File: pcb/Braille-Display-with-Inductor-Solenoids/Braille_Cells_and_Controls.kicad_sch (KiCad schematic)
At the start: 6 parts, among them U26 74HC595, U27 74HC595, U28 74HC595, U29 74HC595, U30 74HC595, U31 74HC595

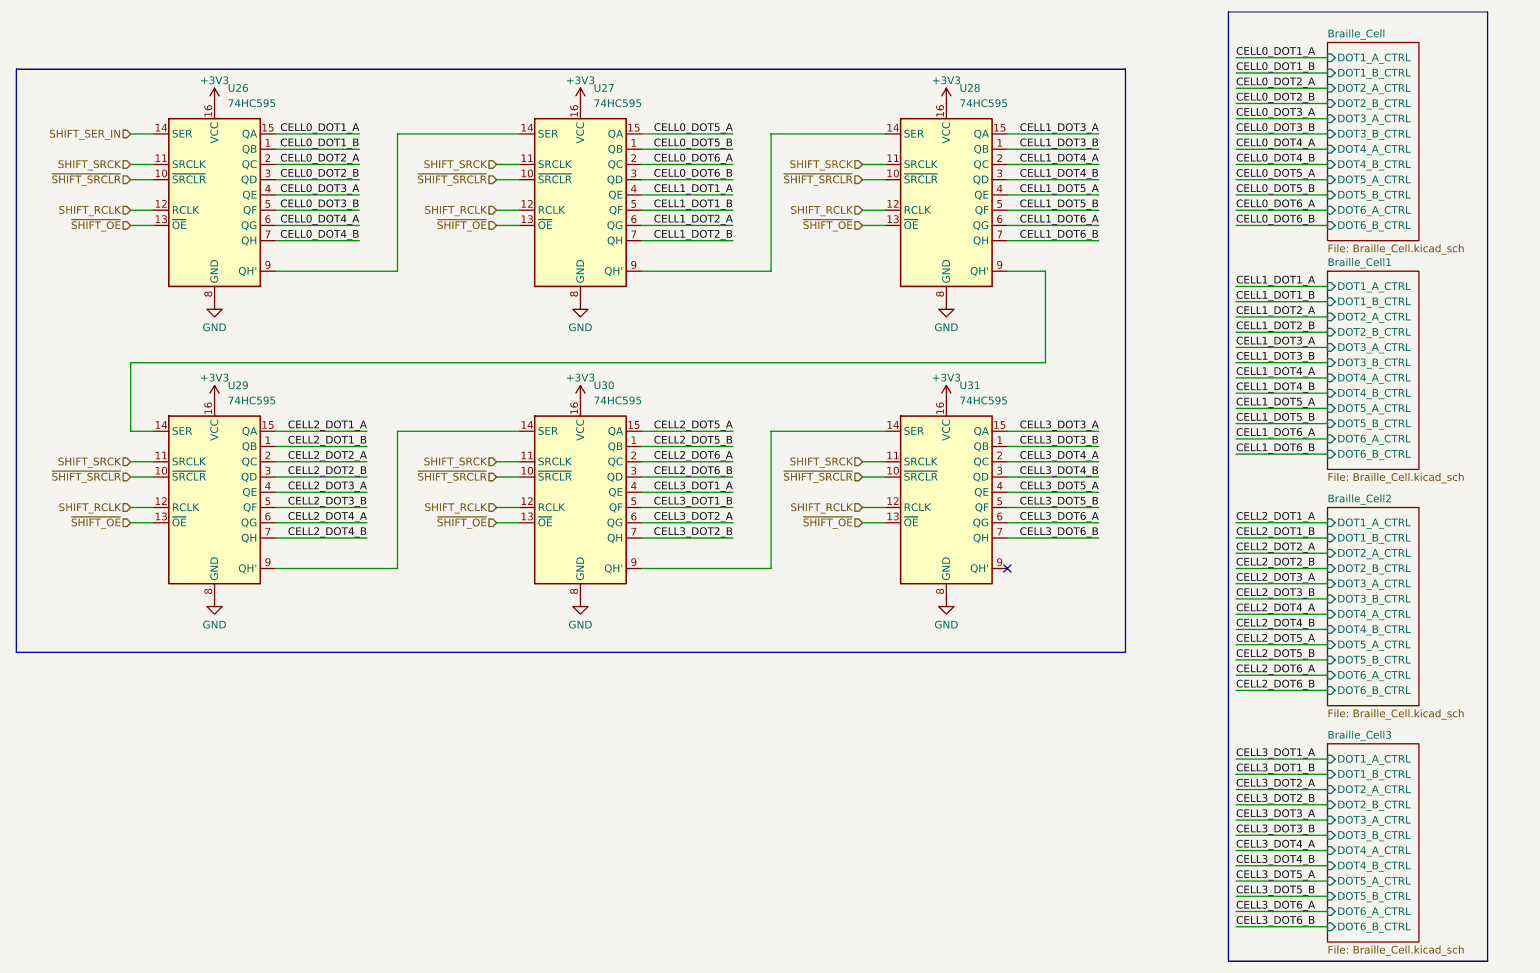
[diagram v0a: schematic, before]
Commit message: WIP (Rev3): Switch to 2 inductors per cell
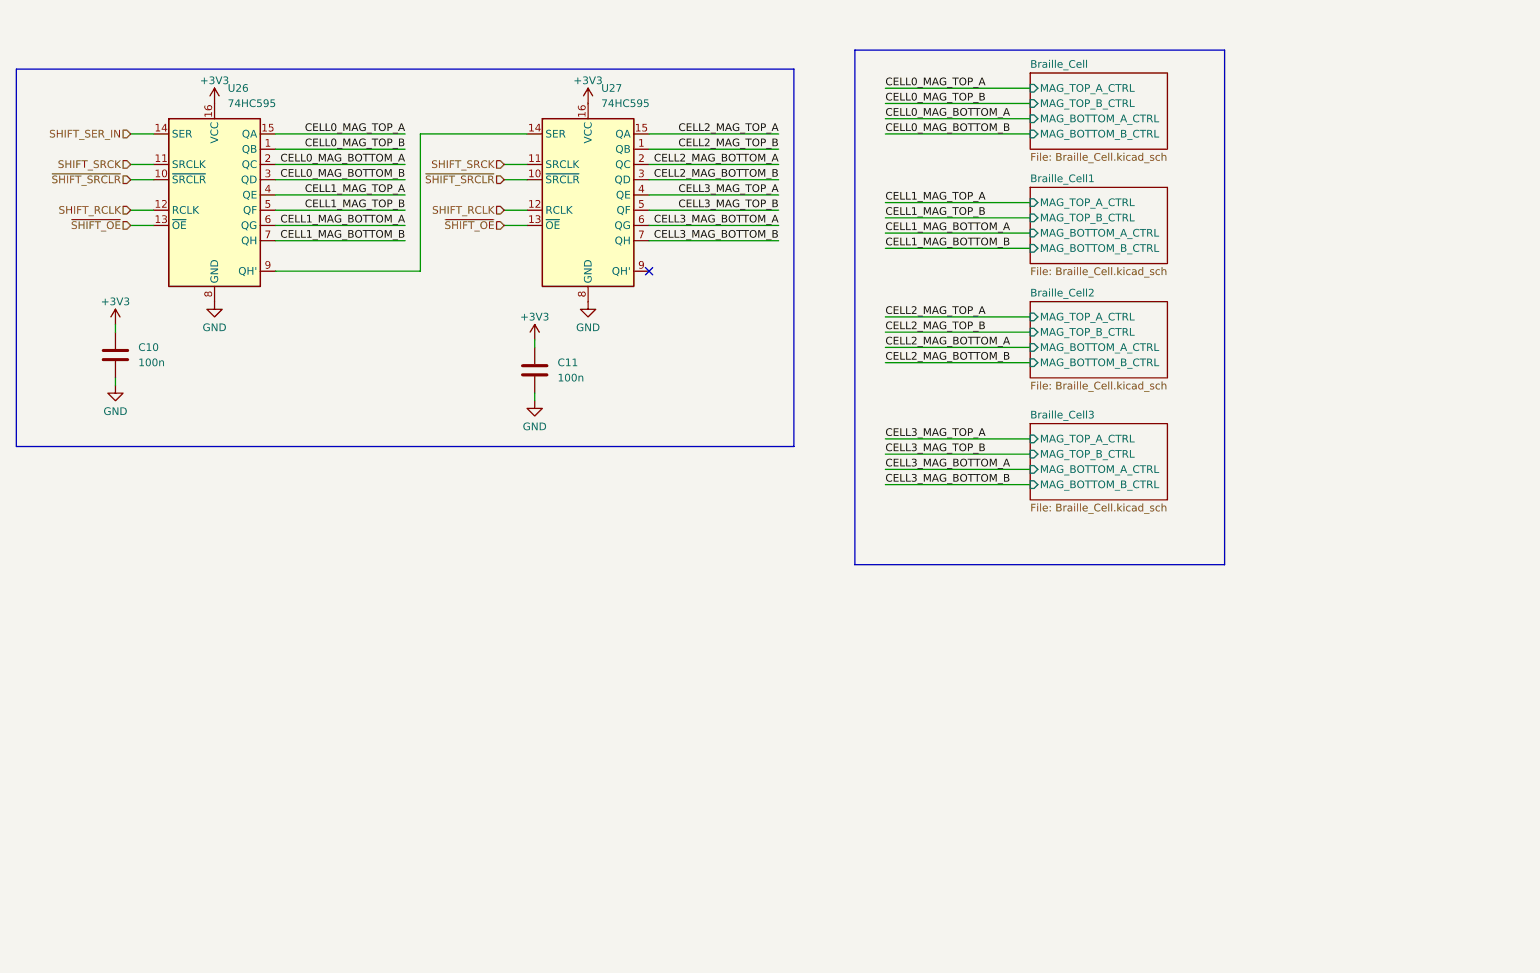
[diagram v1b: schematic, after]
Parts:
- removed U28, U29, U30, U31: 74HC595, Package_SO:SOP-16_3.9x9.9mm_P1.27mm, symbol 74xx:74HC595
- added C10, C11: 100n, Capacitor_SMD:C_1206_3216Metric_Pad1.33x1.80mm_HandSolder, symbol Device:C
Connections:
- net +3V3: now also C10.1, C11.1
- net GND: now also C10.2, C11.2
- net CELL0_DOT1_A renamed CELL0_MAG_TOP_A
- net CELL0_DOT1_B renamed CELL0_MAG_TOP_B
- net CELL0_DOT2_A renamed CELL0_MAG_BOTTOM_A
- net CELL0_DOT2_B renamed CELL0_MAG_BOTTOM_B
- net CELL0_DOT3_A renamed CELL1_MAG_TOP_A
- net CELL0_DOT3_B renamed CELL1_MAG_TOP_B
- net CELL0_DOT4_A renamed CELL1_MAG_BOTTOM_A
- net CELL0_DOT4_B renamed CELL1_MAG_BOTTOM_B
- net CELL0_DOT5_A renamed CELL2_MAG_TOP_A
- net CELL0_DOT5_B renamed CELL2_MAG_TOP_B
- net CELL0_DOT6_A renamed CELL2_MAG_BOTTOM_A
- net CELL0_DOT6_B renamed CELL2_MAG_BOTTOM_B
- net CELL1_DOT1_A renamed CELL3_MAG_TOP_A
- net CELL1_DOT1_B renamed CELL3_MAG_TOP_B
- net CELL1_DOT2_A renamed CELL3_MAG_BOTTOM_A
- net CELL1_DOT2_B renamed CELL3_MAG_BOTTOM_B
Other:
- sheet Braille_Cell ports: added MAG_BOTTOM_A_CTRL, MAG_BOTTOM_B_CTRL, MAG_TOP_A_CTRL, MAG_TOP_B_CTRL; removed DOT1_A_CTRL, DOT1_B_CTRL, DOT2_A_CTRL, DOT2_B_CTRL, DOT3_A_CTRL, DOT3_B_CTRL, DOT4_A_CTRL, DOT4_B_CTRL, DOT5_A_CTRL, DOT5_B_CTRL, DOT6_A_CTRL, DOT6_B_CTRL
- sheet Braille_Cell1 ports: added MAG_BOTTOM_A_CTRL, MAG_BOTTOM_B_CTRL, MAG_TOP_A_CTRL, MAG_TOP_B_CTRL; removed DOT1_A_CTRL, DOT1_B_CTRL, DOT2_A_CTRL, DOT2_B_CTRL, DOT3_A_CTRL, DOT3_B_CTRL, DOT4_A_CTRL, DOT4_B_CTRL, DOT5_A_CTRL, DOT5_B_CTRL, DOT6_A_CTRL, DOT6_B_CTRL
- sheet Braille_Cell2 ports: added MAG_BOTTOM_A_CTRL, MAG_BOTTOM_B_CTRL, MAG_TOP_A_CTRL, MAG_TOP_B_CTRL; removed DOT1_A_CTRL, DOT1_B_CTRL, DOT2_A_CTRL, DOT2_B_CTRL, DOT3_A_CTRL, DOT3_B_CTRL, DOT4_A_CTRL, DOT4_B_CTRL, DOT5_A_CTRL, DOT5_B_CTRL, DOT6_A_CTRL, DOT6_B_CTRL
- sheet Braille_Cell3 ports: added MAG_BOTTOM_A_CTRL, MAG_BOTTOM_B_CTRL, MAG_TOP_A_CTRL, MAG_TOP_B_CTRL; removed DOT1_A_CTRL, DOT1_B_CTRL, DOT2_A_CTRL, DOT2_B_CTRL, DOT3_A_CTRL, DOT3_B_CTRL, DOT4_A_CTRL, DOT4_B_CTRL, DOT5_A_CTRL, DOT5_B_CTRL, DOT6_A_CTRL, DOT6_B_CTRL
- moved on the sheet: U27
